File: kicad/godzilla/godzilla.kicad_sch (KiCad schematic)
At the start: 3 parts, among them U1 NE555P

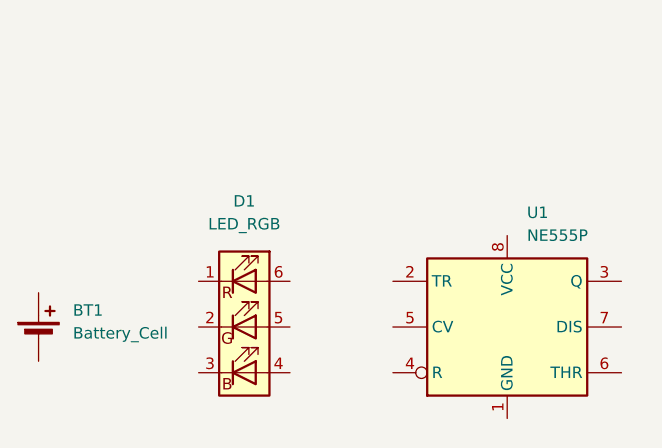
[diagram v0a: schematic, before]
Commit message: Fixed vector timing for stupid DACs
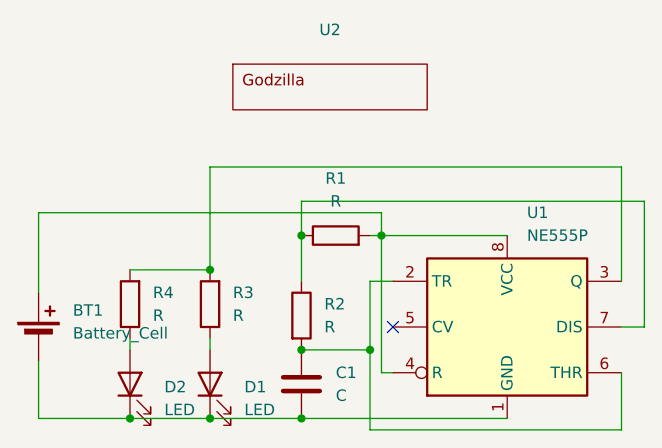
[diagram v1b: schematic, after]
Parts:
- removed D1: LED_RGB, LED_SMD:LED_WS2812_PLCC6_5.0x5.0mm_P1.6mm, symbol Device:LED_RGB
- added C1: C, Capacitor_THT:CP_Radial_D4.0mm_P2.00mm, symbol Device:C
- added D1, D2: LED, LED_SMD:LED_0603_1608Metric_Pad1.05x0.95mm_HandSolder, symbol Device:LED
- added R1, R2, R3, R4: R, custom_footprint_library:0.4_pitch_resistor, symbol Device:R
- added U2: ~, custom_footprint_library:godzilla_silkscreen, symbol custom_symbol_lib:godzilla_placeholder
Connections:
- net at U1.1 (GND): now also BT1.2 (-), C1.2, D1.1 (K), D2.1 (K)
- net at U1.2 (TR): now also U1.6 (THR), C1.1, R2.2
- net at U1.3 (Q): now also R3.2, R4.2
- net at U1.4 (R): now also BT1.1 (+), U1.8 (VCC), R1.2
- net at U1.7 (DIS): now also R1.1, R2.1
- new net: D1.2 (A), R3.1
- new net: D2.2 (A), R4.1
- no-connect marks 0 -> 1
